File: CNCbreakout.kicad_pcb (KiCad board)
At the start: 2 copper layers, 7 parts, among them P1 X1_IN, P10 XY_STOP, P11 Z_STOP, P2 X2_IN, P5 VFD_IN, P6 X1_OUT, P7 X2_OUT

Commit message: started pcb layout
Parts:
- removed P1: X1_IN, Connect:DB25FC
- removed P10: XY_STOP, Connect:DB9FC
- removed P11: Z_STOP, Connect:DB9FC
- removed P2: X2_IN, Connect:DB25FC
- removed P5: VFD_IN, Connect:DB9FC
- removed P6: X1_OUT, Connect:DB25MC
- removed P7: X2_OUT, Connect:DB25MC
- added D201: LED, LEDs:LED_1206, F.Cu at (279.4, 102.9)
- added D202: LED, LEDs:LED_1206, F.Cu at (269.2, 102.9)
- added D203: LED, LEDs:LED_1206, F.Cu at (259.1, 102.9)
- added D204: LED, LEDs:LED_1206, F.Cu at (248.9, 102.9)
- added D205: LED, LEDs:LED_1206, F.Cu at (238.8, 102.9)
- added D206: LED, LEDs:LED_1206, F.Cu at (228.6, 102.9)
- added D301: LED, LEDs:LED_1206, F.Cu at (39.4, 66.0)
- added D302: LED, LEDs:LED_1206, F.Cu at (57.1, 66.0)
- added D303: LED, LEDs:LED_1206, F.Cu at (96.5, 64.8)
- added D304: LED, LEDs:LED_1206, F.Cu at (114.3, 64.8)
- added D305: LED, LEDs:LED_1206, F.Cu at (151.1, 64.8)
- added D306: LED, LEDs:LED_1206, F.Cu at (166.4, 64.8)
- added D307: LED, LEDs:LED_1206, F.Cu at (39.4, 58.4)
- added D308: LED, LEDs:LED_1206, F.Cu at (57.1, 58.4)
- added D309: LED, LEDs:LED_1206, F.Cu at (96.5, 58.4)
- added D310: LED, LEDs:LED_1206, F.Cu at (114.3, 58.4)
- added D311: LED, LEDs:LED_1206, F.Cu at (151.1, 58.4)
- added D312: LED, LEDs:LED_1206, F.Cu at (166.4, 58.4)
- added D313: LED, LEDs:LED_1206, F.Cu at (158.8, 62.2)
- added D314: LED, LEDs:LED_1206, F.Cu at (48.3, 62.2)
- added D315: LED, LEDs:LED_1206, F.Cu at (105.4, 62.2)
- added P101: X1, Connect:DB9FC, F.Cu at (47.0, 133.3)
- added P102: X2, Connect:DB9FC, F.Cu at (85.1, 133.3)
- added P103: Y, Connect:DB9FC, F.Cu at (123.2, 133.3)
- added P104: Z, Connect:DB9FC, F.Cu at (161.3, 133.3)
- added P105: GND, Connect:bornier2, F.Cu at (256.5, 48.3)
- added P106: +24V, Connect:bornier2, F.Cu at (268.0, 33.0)
- added P110: CONN_01X02, Connect:bornier2, F.Cu at (273.1, 77.5)
- added P111: CONN_01X02, Connect:bornier2, F.Cu at (254.0, 77.5)
- added P112: CONN_01X02, Connect:bornier2, F.Cu at (233.7, 77.5)
- added Q201: Q_NMOS_GDS, TO_SOT_Packages_SMD:TO-252-2Lead, F.Cu at (279.4, 95.2)
- added Q202: Q_NMOS_GDS, TO_SOT_Packages_SMD:TO-252-2Lead, F.Cu at (269.2, 95.2)
- added Q203: Q_NMOS_GDS, TO_SOT_Packages_SMD:TO-252-2Lead, F.Cu at (259.1, 95.2)
- added Q204: Q_NMOS_GDS, TO_SOT_Packages_SMD:TO-252-2Lead, F.Cu at (248.9, 95.2)
- added Q205: Q_NMOS_GDS, TO_SOT_Packages_SMD:TO-252-2Lead, F.Cu at (238.8, 95.2)
- added Q206: Q_NMOS_GDS, TO_SOT_Packages_SMD:TO-252-2Lead, F.Cu at (228.6, 95.2)
- added Q301: Q_NPN_CBE, TO_SOT_Packages_SMD:SOT-23, F.Cu at (41.9, 96.5)
- added Q302: Q_NPN_CBE, TO_SOT_Packages_SMD:SOT-23, F.Cu at (61.0, 96.5)
- added Q303: Q_NPN_CBE, TO_SOT_Packages_SMD:SOT-23, F.Cu at (43.2, 83.8)
- added Q304: Q_NPN_CBE, TO_SOT_Packages_SMD:SOT-23, F.Cu at (61.0, 83.8)
- added Q305: Q_NPN_CBE, TO_SOT_Packages_SMD:SOT-23, F.Cu at (95.2, 85.1)
- added Q306: Q_NPN_CBE, TO_SOT_Packages_SMD:SOT-23, F.Cu at (114.3, 85.1)
- added Q307: Q_NPN_CBE, TO_SOT_Packages_SMD:SOT-23, F.Cu at (149.9, 85.1)
- added Q308: Q_NPN_CBE, TO_SOT_Packages_SMD:SOT-23, F.Cu at (167.6, 85.1)
- added R201: 2K, Resistors_SMD:R_1206, F.Cu at (278.1, 99.1)
- added R202: 2K, Resistors_SMD:R_1206, F.Cu at (276.9, 108.0)
- added R203: 2K, Resistors_SMD:R_1206, F.Cu at (268.0, 99.1)
- added R204: 2K, Resistors_SMD:R_1206, F.Cu at (266.7, 108.0)
- added R205: 2K, Resistors_SMD:R_1206, F.Cu at (257.8, 99.1)
- added R206: 2K, Resistors_SMD:R_1206, F.Cu at (256.5, 108.0)
- added R207: 2K, Resistors_SMD:R_1206, F.Cu at (247.7, 99.1)
- added R208: 2K, Resistors_SMD:R_1206, F.Cu at (246.4, 108.0)
- added R209: 2K, Resistors_SMD:R_1206, F.Cu at (237.5, 99.1)
- added R210: 2K, Resistors_SMD:R_1206, F.Cu at (236.2, 108.0)
- added R211: 2K, Resistors_SMD:R_1206, F.Cu at (227.3, 99.1)
- added R212: 2K, Resistors_SMD:R_1206, F.Cu at (226.1, 108.0)
- added R303: 5K, Resistors_SMD:R_1206, F.Cu at (40.6, 90.2)
- added R304: 5K, Resistors_SMD:R_1206, F.Cu at (58.4, 90.2)
- added R305: 5K, Resistors_SMD:R_1206, F.Cu at (92.7, 92.7)
- added R306: 5K, Resistors_SMD:R_1206, F.Cu at (111.8, 92.7)
- added R307: 5K, Resistors_SMD:R_1206, F.Cu at (147.3, 92.7)
- added R308: 5K, Resistors_SMD:R_1206, F.Cu at (165.1, 92.7)
- added R309: 5K, Resistors_SMD:R_1206, F.Cu at (41.9, 72.4)
- added R310: 5K, Resistors_SMD:R_1206, F.Cu at (55.9, 72.4)
- added R311: 5K, Resistors_SMD:R_1206, F.Cu at (100.3, 71.1)
- added R312: 5K, Resistors_SMD:R_1206, F.Cu at (113.0, 71.1)
- added R313: 5K, Resistors_SMD:R_1206, F.Cu at (153.7, 71.1)
- added R314: 5K, Resistors_SMD:R_1206, F.Cu at (166.4, 71.1)
- added R315: 2K5, Resistors_SMD:R_1206, F.Cu at (45.7, 90.2)
- added R316: 2K5, Resistors_SMD:R_1206, F.Cu at (63.5, 90.2)
- added R317: 5K, Resistors_SMD:R_1206, F.Cu at (97.8, 92.7)
- added R318: 5K, Resistors_SMD:R_1206, F.Cu at (116.8, 92.7)
- added R319: 5K, Resistors_SMD:R_1206, F.Cu at (152.4, 92.7)
- added R320: 5K, Resistors_SMD:R_1206, F.Cu at (170.2, 92.7)
- added R321: 10K, Resistors_SMD:R_1206, F.Cu at (48.3, 83.8)
- added R322: 10K, Resistors_SMD:R_1206, F.Cu at (66.0, 83.8)
- added R323: 10K, Resistors_SMD:R_1206, F.Cu at (100.3, 85.1)
- added R324: 10K, Resistors_SMD:R_1206, F.Cu at (119.4, 85.1)
- added R325: 10K, Resistors_SMD:R_1206, F.Cu at (154.9, 85.1)
- added R326: 10K, Resistors_SMD:R_1206, F.Cu at (172.7, 85.1)
- added R327: 10K, Resistors_SMD:R_1206, F.Cu at (35.6, 72.4)
- added R328: 10K, Resistors_SMD:R_1206, F.Cu at (61.0, 72.4)
- added R329: 10K, Resistors_SMD:R_1206, F.Cu at (94.0, 71.1)
- added R330: 10K, Resistors_SMD:R_1206, F.Cu at (118.1, 71.1)
- added R331: 10K, Resistors_SMD:R_1206, F.Cu at (147.3, 71.1)
- added R332: 10K, Resistors_SMD:R_1206, F.Cu at (172.7, 71.1)
- added R333: 10K, Resistors_SMD:R_1206, F.Cu at (194.3, 26.7)
- added R334: 10K, Resistors_SMD:R_1206, F.Cu at (194.3, 33.0)
- added R335: 10K, Resistors_SMD:R_1206, F.Cu at (106.7, 71.1)
- added R336: 10K, Resistors_SMD:R_1206, F.Cu at (160.0, 71.1)
- added R337: 10K, Resistors_SMD:R_1206, F.Cu at (49.5, 72.4)
- added R338: 100K, Resistors_SMD:R_1206, F.Cu at (212.1, 33.0)
- added R339: 100K, Resistors_SMD:R_1206, F.Cu at (212.1, 26.7)
- added U301: 4N25, Opto-Devices:Optocoupler_SMD_ReflowWaveSoldering_KPC357_LTV35x_PC357_SingleChannel, F.Cu at (203.2, 27.9)
- added U302: 4N25, Opto-Devices:Optocoupler_SMD_ReflowWaveSoldering_KPC357_LTV35x_PC357_SingleChannel, F.Cu at (203.2, 34.3)

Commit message: added opto and DE footprints
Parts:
- added P107: Z_STOP, CNCbreakout:DE15HDFC, F.Cu at (22.9, 48.3)
- added P108: XY_STOP, CNCbreakout:DE15HDFC, F.Cu at (22.9, 96.5)
- added P109: VFD_IN, CNCbreakout:DE15HDFC, F.Cu at (207.0, 138.4)
- added R601: R, Resistors_SMD:R_1206, F.Cu at (35.6, 120.7)
- added R602: R, Resistors_SMD:R_1206, F.Cu at (73.7, 120.7)
- added R603: R, Resistors_SMD:R_1206, F.Cu at (111.8, 120.7)
- added R604: R, Resistors_SMD:R_1206, F.Cu at (151.1, 120.7)
- added U601: TCMT1108, CNCbreakout:TCMT1108, F.Cu at (36.8, 124.5)
- added U602: TCMT1108, CNCbreakout:TCMT1108, F.Cu at (74.9, 124.5)
- added U603: TCMT1108, CNCbreakout:TCMT1108, F.Cu at (113.0, 124.5)
- added U604: TCMT1108, CNCbreakout:TCMT1108, F.Cu at (152.4, 124.5)
- P101, P102, P103, P104: footprint Connect:DB9FC -> CNCbreakout:DE9FC
- U301, U302: value 4N25 -> TCMT1108; footprint Opto-Devices:Optocoupler_SMD_ReflowWaveSoldering_KPC357_LTV35x_PC357_SingleChannel -> CNCbreakout:TCMT1108
- moved R202 66.1 mm to (210.8, 109.2), turned to 180 degrees
- moved D201 64.1 mm to (215.9, 111.8), turned to 90 degrees
- moved R201 59.5 mm to (219.7, 110.5), turned to 90 degrees
- moved Q201 58.3 mm to (223.5, 111.8), turned to 270 degrees
- moved R204 56.6 mm to (210.8, 99.1), turned to 180 degrees
- moved D202 53.4 mm to (215.9, 101.6), turned to 90 degrees
- moved R212 51.8 mm to (210.8, 58.4), turned to 180 degrees
- moved R206 49.5 mm to (210.8, 88.9), turned to 180 degrees
- moved R203 48.3 mm to (219.7, 100.3), turned to 90 degrees
- moved R210 46.9 mm to (210.8, 68.6), turned to 180 degrees
- moved Q202 46.2 mm to (223.5, 101.6), turned to 270 degrees
- moved R208 46.0 mm to (210.8, 78.7), turned to 180 degrees
- moved D203 44.7 mm to (215.9, 91.4), turned to 90 degrees
- moved D206 43.8 mm to (215.9, 61.0), turned to 270 degrees
- moved P110 42.3 mm to (241.3, 105.4), turned to 270 degrees
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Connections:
- P101 pad 4: Net-(P101-Pad4) -> /Estop_Logic/X1EN+
- P101 pad 5: Net-(P101-Pad5) -> /Estop_Logic/X1EN-
- P102 pad 4: Net-(P102-Pad4) -> /Estop_Logic/X2EN+
- P102 pad 5: Net-(P102-Pad5) -> /Estop_Logic/X2EN-
- P103 pad 4: Net-(P103-Pad4) -> /Estop_Logic/YEN+
- P103 pad 5: Net-(P103-Pad5) -> /Estop_Logic/YEN-
- P104 pad 4: Net-(P104-Pad4) -> /Estop_Logic/ZEN+
- P104 pad 5: Net-(P104-Pad5) -> /Estop_Logic/ZEN-
- U301 pad 3: (no net) -> DGND
- U301 pad 4: DGND -> DOut_1
- U302 pad 3: (no net) -> DGND
- U302 pad 4: DGND -> DOut_2

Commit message: set limits to pull down, optional invert
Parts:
- added D316: ZENERsmall, Diodes_SMD:SOD-123, F.Cu at (123.0, 82.0)
- added D317: ZENERsmall, Diodes_SMD:SOD-123, F.Cu at (147.0, 82.0)
- added D318: ZENERsmall, Diodes_SMD:SOD-123, F.Cu at (171.0, 82.0)
- added D319: LED, LEDs:LED_1206, F.Cu at (153.0, 69.0)
- added D320: LED, LEDs:LED_1206, F.Cu at (57.0, 69.0)
- added D321: LED, LEDs:LED_1206, F.Cu at (105.0, 69.0)
- added JP301: JUMPER3, CNCbreakout:JumperDouble, F.Cu at (44.0, 89.0)
- added JP302: JUMPER3, CNCbreakout:JumperDouble, F.Cu at (68.0, 89.0)
- added JP303: JUMPER3, CNCbreakout:JumperDouble, F.Cu at (92.0, 89.0)
- added JP304: JUMPER3, CNCbreakout:JumperDouble, F.Cu at (116.0, 89.0)
- added JP305: JUMPER3, CNCbreakout:JumperDouble, F.Cu at (140.0, 89.0)
- added JP306: JUMPER3, CNCbreakout:JumperDouble, F.Cu at (164.0, 89.0)
- added Q309: Q_NPN_CBE, TO_SOT_Packages_SMD:SOT-23, F.Cu at (98.0, 94.0)
- added Q310: Q_NPN_CBE, TO_SOT_Packages_SMD:SOT-23, F.Cu at (122.0, 94.0)
- added Q311: Q_NPN_CBE, TO_SOT_Packages_SMD:SOT-23, F.Cu at (146.0, 94.0)
- added Q312: Q_NPN_CBE, TO_SOT_Packages_SMD:SOT-23, F.Cu at (170.0, 94.0)
- added Q313: Q_NPN_CBE, TO_SOT_Packages_SMD:SOT-23, F.Cu at (50.0, 86.0)
- added Q314: Q_NPN_CBE, TO_SOT_Packages_SMD:SOT-23, F.Cu at (74.0, 86.0)
- added Q315: Q_NPN_CBE, TO_SOT_Packages_SMD:SOT-23, F.Cu at (98.0, 86.0)
- added Q316: Q_NPN_CBE, TO_SOT_Packages_SMD:SOT-23, F.Cu at (122.0, 86.0)
- added Q317: Q_NPN_CBE, TO_SOT_Packages_SMD:SOT-23, F.Cu at (146.0, 86.0)
- added Q318: Q_NPN_CBE, TO_SOT_Packages_SMD:SOT-23, F.Cu at (170.0, 86.0)
- added R301: 5K, Resistors_SMD:R_1206, F.Cu at (44.0, 100.0)
- added R302: 5K, Resistors_SMD:R_1206, F.Cu at (68.0, 100.0)
- added R340: 5K, Resistors_SMD:R_1206, F.Cu at (111.0, 79.0)
- added R341: 5K, Resistors_SMD:R_1206, F.Cu at (135.0, 79.0)
- added R342: 5K, Resistors_SMD:R_1206, F.Cu at (159.0, 79.0)
- added R343: 10K, Resistors_SMD:R_1206, F.Cu at (47.0, 79.0)
- added R344: 10K, Resistors_SMD:R_1206, F.Cu at (71.0, 79.0)
- added R345: 10K, Resistors_SMD:R_1206, F.Cu at (95.0, 79.0)
- added R346: 10K, Resistors_SMD:R_1206, F.Cu at (119.0, 79.0)
- added R347: 10K, Resistors_SMD:R_1206, F.Cu at (143.0, 79.0)
- added R348: 10K, Resistors_SMD:R_1206, F.Cu at (167.0, 79.0)
- added R349: 10K, Resistors_SMD:R_1206, F.Cu at (207.5, 117.5)
- added R350: 10K, Resistors_SMD:R_1206, F.Cu at (201.5, 118.0)
- added R351: 10K, Resistors_SMD:R_1206, F.Cu at (108.0, 75.0)
- added R352: 10K, Resistors_SMD:R_1206, F.Cu at (156.0, 75.0)
- added R353: 10K, Resistors_SMD:R_1206, F.Cu at (60.0, 75.0)
- D313, D314, D315: value LED -> ZENERsmall; footprint LEDs:LED_1206 -> Diodes_SMD:SOD-123
- P107: value Z_STOP -> CONN_01X02; footprint CNCbreakout:DE15HDFC -> Connect:bornier2
- P108: value XY_STOP -> CONN_01X02; footprint CNCbreakout:DE15HDFC -> Connect:bornier2
- P109: value VFD_IN -> CONN_01X02; footprint CNCbreakout:DE15HDFC -> Connect:bornier2
- P110: value CONN_01X02 -> Z_STOP; footprint Connect:bornier2 -> CNCbreakout:DE15HDFC
- P111: value CONN_01X02 -> XY_STOP; footprint Connect:bornier2 -> CNCbreakout:DE15HDFC
- P112: value CONN_01X02 -> VFD_IN; footprint Connect:bornier2 -> CNCbreakout:DE15HDFC
- R307, R308, R309, R310, R311, R312: value 5K -> 20K
- R313, R314, R317, R318: value 5K -> 10K
- R315, R316: value 2K5 -> 10K
- R321, R322, R323, R324, R331, R332, R333, R334, R335, R336: value 10K -> 5K
- R338: value 100K -> 10K
- R339: value 100K -> 5K
- moved P107 228.8 mm to (244.0, 107.0), turned to 270 degrees
- moved P111 224.7 mm to (18.0, 111.0), turned to 90 degrees
- moved P110 224.1 mm to (19.0, 77.0), turned to 90 degrees
- moved P108 221.4 mm to (244.0, 85.5), turned to 270 degrees
- moved R338 156.0 mm to (63.0, 79.0)
- moved R339 135.6 mm to (87.0, 79.0)
- moved R333 121.2 mm to (87.0, 83.0), turned to 0 degrees
- moved R313 114.8 mm to (39.0, 89.0)
- moved R319 113.4 mm to (39.0, 95.0), turned to 180 degrees
- moved D313 109.5 mm to (51.0, 82.0), turned to 180 degrees
- moved R332 109.1 mm to (63.0, 83.0), turned to 0 degrees
- moved R307 108.5 mm to (39.0, 99.0), turned to 0 degrees
- moved R331 107.7 mm to (39.0, 83.0), turned to 180 degrees
- moved R320 107.2 mm to (63.0, 95.0), turned to 180 degrees
- moved R314 103.7 mm to (63.0, 89.0)
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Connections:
- D307 pad 1: Net-(D307-Pad1) -> GND
- D307 pad 2: LimX+ -> Net-(D307-Pad2)
- D308 pad 1: Net-(D308-Pad1) -> GND
- D308 pad 2: LimX- -> Net-(D308-Pad2)
- D309 pad 1: Net-(D309-Pad1) -> GND
- D309 pad 2: LimY+ -> Net-(D309-Pad2)
- D310 pad 1: Net-(D310-Pad1) -> GND
- D310 pad 2: LimY- -> Net-(D310-Pad2)
- D311 pad 1: Net-(D311-Pad1) -> GND
- D311 pad 2: LimZ+ -> Net-(D311-Pad2)
- D312 pad 1: Net-(D312-Pad1) -> GND
- D312 pad 2: LimZ- -> Net-(D312-Pad2)
- D313 pad 1: HomeZ -> Net-(D313-Pad1)
- D313 pad 2: Net-(D313-Pad2) -> GND
- D314 pad 1: HomeX -> Net-(D314-Pad1)
- D314 pad 2: Net-(D314-Pad2) -> GND
- D315 pad 1: HomeY -> Net-(D315-Pad1)
- D315 pad 2: Net-(D315-Pad2) -> GND
- P101 pad 6: +24V -> Net-(P101-Pad6)
- P102 pad 6: +24V -> Net-(P102-Pad6)
- P103 pad 6: +24V -> Net-(P103-Pad6)
- P104 pad 6: +24V -> Net-(P104-Pad6)
- P107 pad 1: GND -> /vfd_aux/GPO2
- P107 pad 2: SOL1 -> /vfd_aux/GPO1
- P108 pad 1: GND -> /vfd_aux/GPO4
- P108 pad 2: LimY+ -> /vfd_aux/GPO3
- P109 pad 1: +24V -> /vfd_aux/GPO6
- P109 pad 2: DIn_1 -> /vfd_aux/GPO5
- P110 pad 1: /vfd_aux/GPO2 -> GND
- P110 pad 2: /vfd_aux/GPO1 -> SOL1
- P111 pad 1: /vfd_aux/GPO4 -> GND
- P111 pad 2: /vfd_aux/GPO3 -> LimY+
- P112 pad 1: /vfd_aux/GPO6 -> +24V
- P112 pad 2: /vfd_aux/GPO5 -> DIn_1
- Q303 pad 1: Net-(Q303-Pad1) -> Y+Lim
- Q304 pad 1: Net-(Q304-Pad1) -> Y-Lim
- Q305 pad 1: Net-(Q305-Pad1) -> Z+Lim
- Q306 pad 1: Net-(Q306-Pad1) -> Z-Lim
- Q307 pad 1: Net-(Q307-Pad1) -> Net-(D301-Pad2)
- Q308 pad 1: Net-(Q308-Pad1) -> Net-(D302-Pad2)
- R303 pad 1: Net-(Q303-Pad1) -> Y+Lim
- R303 pad 2: Net-(Q301-Pad2) -> GND
- R304 pad 1: Net-(Q304-Pad1) -> Y-Lim
- R304 pad 2: Net-(Q302-Pad2) -> GND
- R305 pad 1: Net-(Q305-Pad1) -> Z+Lim
- R305 pad 2: Y+Lim -> GND
- R306 pad 1: Net-(Q306-Pad1) -> Z-Lim
- R306 pad 2: Y-Lim -> GND
- R307 pad 1: Net-(Q307-Pad1) -> +24V
- R307 pad 2: Z+Lim -> F1_LIM
- R308 pad 1: Net-(Q308-Pad1) -> +24V
- R308 pad 2: Z-Lim -> R1_LIM
- R309 pad 1: Net-(D301-Pad2) -> +24V
- R309 pad 2: Net-(Q303-Pad1) -> Y+Lim
- R310 pad 1: Net-(D302-Pad2) -> +24V
- R310 pad 2: Net-(Q304-Pad1) -> Y-Lim
- R311 pad 1: Net-(D303-Pad2) -> +24V
- R311 pad 2: Net-(Q305-Pad1) -> Z+Lim
- R312 pad 1: Net-(D304-Pad2) -> +24V
- R312 pad 2: Net-(Q306-Pad1) -> Z-Lim
- R313 pad 1: Net-(D305-Pad2) -> Net-(JP301-Pad2)
- R313 pad 2: Net-(Q307-Pad1) -> Net-(Q301-Pad2)
- R314 pad 1: Net-(D306-Pad2) -> Net-(JP302-Pad2)
- R314 pad 2: Net-(Q308-Pad1) -> Net-(Q302-Pad2)
- R315 pad 1: +24V -> Net-(JP303-Pad2)
- R315 pad 2: Net-(Q303-Pad1) -> Net-(Q303-Pad2)
- R316 pad 1: +24V -> Net-(JP304-Pad2)
- R316 pad 2: Net-(Q304-Pad1) -> Net-(Q304-Pad2)
- R317 pad 1: +24V -> Net-(JP305-Pad2)
- R317 pad 2: Net-(Q305-Pad1) -> Net-(Q305-Pad2)
- R318 pad 1: +24V -> Net-(JP306-Pad2)
- R318 pad 2: Net-(Q306-Pad1) -> Net-(Q306-Pad2)
- R319 pad 1: +24V -> Net-(D301-Pad2)
- R319 pad 2: Net-(Q307-Pad1) -> +24V
- R320 pad 1: +24V -> Net-(D302-Pad2)
- R320 pad 2: Net-(Q308-Pad1) -> +24V
- R321 pad 1: Net-(Q303-Pad2) -> +24V
- R321 pad 2: GND -> Net-(D303-Pad2)
- R322 pad 1: Net-(Q304-Pad2) -> +24V
- R322 pad 2: GND -> Net-(D304-Pad2)
- R323 pad 1: Net-(Q305-Pad2) -> +24V
- R323 pad 2: GND -> Net-(D305-Pad2)
- R324 pad 1: Net-(Q306-Pad2) -> +24V
- R324 pad 2: GND -> Net-(D306-Pad2)
- R325 pad 1: Net-(Q307-Pad2) -> Net-(D307-Pad2)
- R325 pad 2: GND -> Net-(Q307-Pad2)
- R326 pad 1: Net-(Q308-Pad2) -> Net-(D308-Pad2)
- R326 pad 2: GND -> Net-(Q308-Pad2)
- R327 pad 1: Net-(D307-Pad1) -> Net-(D309-Pad2)
- R327 pad 2: Net-(Q303-Pad2) -> Net-(Q309-Pad2)
- R328 pad 1: Net-(D308-Pad1) -> Net-(D310-Pad2)
- R328 pad 2: Net-(Q304-Pad2) -> Net-(Q310-Pad2)
- R329 pad 1: Net-(D309-Pad1) -> Net-(D311-Pad2)
- R329 pad 2: Net-(Q305-Pad2) -> Net-(Q311-Pad2)
- R330 pad 1: Net-(D310-Pad1) -> Net-(D312-Pad2)
- R330 pad 2: Net-(Q306-Pad2) -> Net-(Q312-Pad2)
- R331 pad 1: Net-(D311-Pad1) -> Net-(D307-Pad2)
- R331 pad 2: Net-(Q307-Pad2) -> +24V
- R332 pad 1: Net-(D312-Pad1) -> +24V
- R332 pad 2: Net-(Q308-Pad2) -> Net-(D308-Pad2)
- R333 pad 1: Net-(R333-Pad1) -> +24V
- R333 pad 2: +24V -> Net-(D309-Pad2)
- R334 pad 1: Net-(R334-Pad1) -> +24V
- R334 pad 2: +24V -> Net-(D310-Pad2)
- R335 pad 2: Net-(D315-Pad2) -> Net-(D311-Pad2)
- R336 pad 2: Net-(D313-Pad2) -> Net-(D312-Pad2)
- R337 pad 1: +24V -> LimX+
- R337 pad 2: Net-(D314-Pad2) -> +24V
- R338 pad 1: Net-(R338-Pad1) -> LimX-
- R338 pad 2: DGND -> +24V
- R339 pad 1: Net-(R339-Pad1) -> LimY+
- R339 pad 2: DGND -> +24V
- U301 pad 1: Net-(R333-Pad1) -> Net-(R349-Pad1)
- U302 pad 1: Net-(R334-Pad1) -> Net-(R350-Pad1)
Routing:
- net GND: track 0.00 -> 370.9 mm
- net +24V: track 0.00 -> 136.1 mm
- net Net-(Q301-Pad2): track 0.00 -> 23.8 mm
- net Net-(Q304-Pad2): track 0.00 -> 23.8 mm
- net Net-(Q303-Pad2): track 0.00 -> 23.8 mm
- net Net-(Q302-Pad2): track 0.00 -> 23.8 mm
- net Net-(Q306-Pad2): track 0.00 -> 23.8 mm
- net Net-(Q305-Pad2): track 0.00 -> 23.8 mm
- net Net-(D308-Pad2): track 0.00 -> 19.0 mm
- net Net-(D312-Pad2): track 0.00 -> 19.0 mm
- net Net-(D311-Pad2): track 0.00 -> 19.0 mm
- net Net-(D307-Pad2): track 0.00 -> 19.0 mm
- net Net-(D310-Pad2): track 0.00 -> 19.0 mm
- net Net-(D309-Pad2): track 0.00 -> 19.0 mm
- net Net-(D306-Pad2): track 0.00 -> 16.2 mm
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
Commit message: closer to full routing
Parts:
- P101, P102, P103, P104, P105, P106, P107, P108, P109, P110, P111, P112: moved to B.Cu
- moved P106 90.3 mm to (202.0, 113.0)
- moved P105 70.5 mm to (202.0, 103.0)
- moved R349 45.3 mm to (164.0, 130.0)
- moved D206 45.0 mm to (172.0, 71.0), turned to 90 degrees
- moved R211 44.9 mm to (176.0, 70.0)
- moved Q206 44.7 mm to (180.0, 71.0)
- moved D205 44.6 mm to (172.0, 79.0)
- moved R209 44.5 mm to (176.0, 78.0)
- moved P107 44.3 mm to (202.0, 93.0)
- moved D204 44.3 mm to (172.0, 87.0)
- moved Q205 44.2 mm to (180.0, 79.0)
- moved R207 44.1 mm to (176.0, 86.0)
- moved D203 44.0 mm to (172.0, 95.0)
- moved D202 43.9 mm to (172.0, 103.0)
- moved D201 43.9 mm to (172.0, 111.0)
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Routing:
- net LimZ-: track 5.10 -> 138.7 mm, vias 0 -> 2
- net LimY-: track 5.10 -> 121.2 mm, vias 0 -> 2
- net GND: track 370.9 -> 481.6 mm, vias 0 -> 6
- net LimZ+: track 5.10 -> 113.7 mm
- net LimY+: track 5.10 -> 95.7 mm
- net HomeX: track 0.00 -> 86.3 mm, vias 0 -> 2
- net LimX-: track 5.10 -> 79.2 mm, vias 0 -> 2
- net F1_LIM: track 8.80 -> 75.4 mm, vias 0 -> 2
- net R1_LIM: track 8.80 -> 73.9 mm
- net DIn_6: track 0.00 -> 62.3 mm
- net HomeY: track 0.00 -> 59.2 mm
- net HomeZ: track 0.00 -> 52.2 mm
- net DIn_5: track 0.00 -> 51.9 mm
- net LimX+: track 5.10 -> 54.2 mm
- net Y+Lim: track 8.80 -> 53.3 mm
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
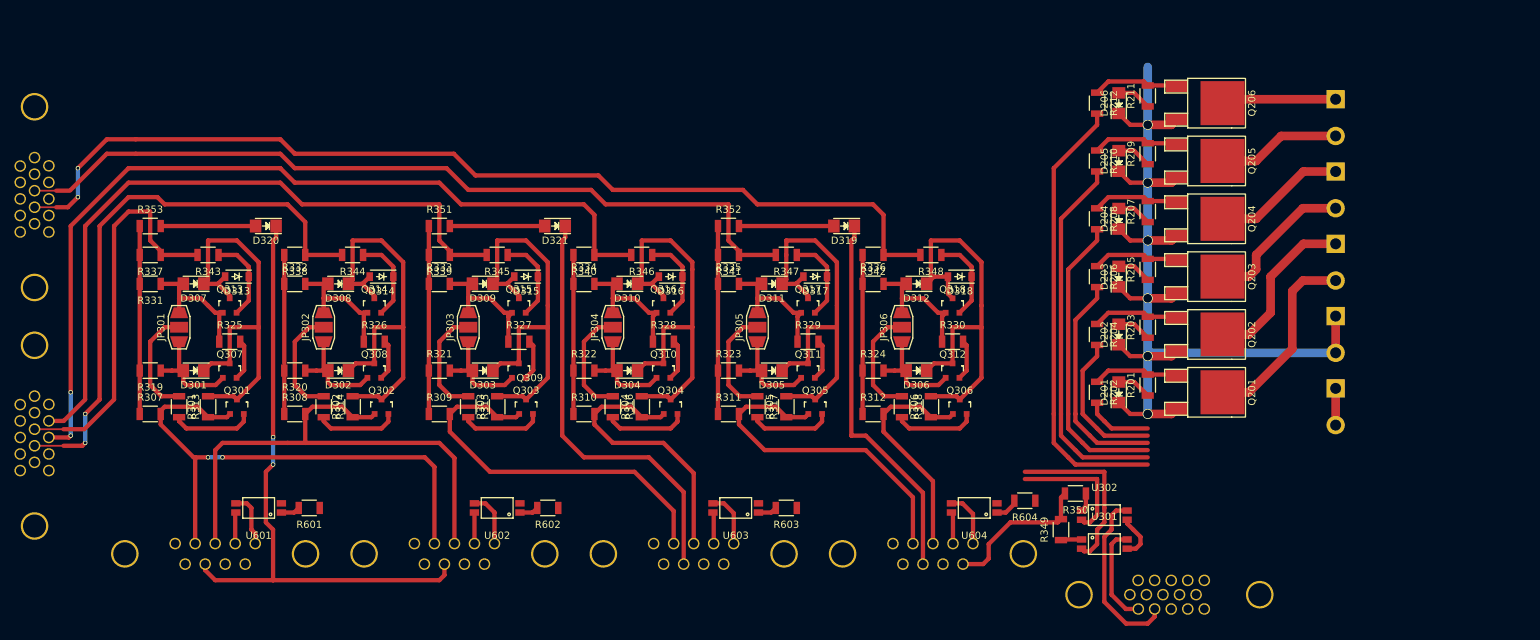
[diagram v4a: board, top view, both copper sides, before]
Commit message: adjusted DE15 footprint, added aux Z-stage lines
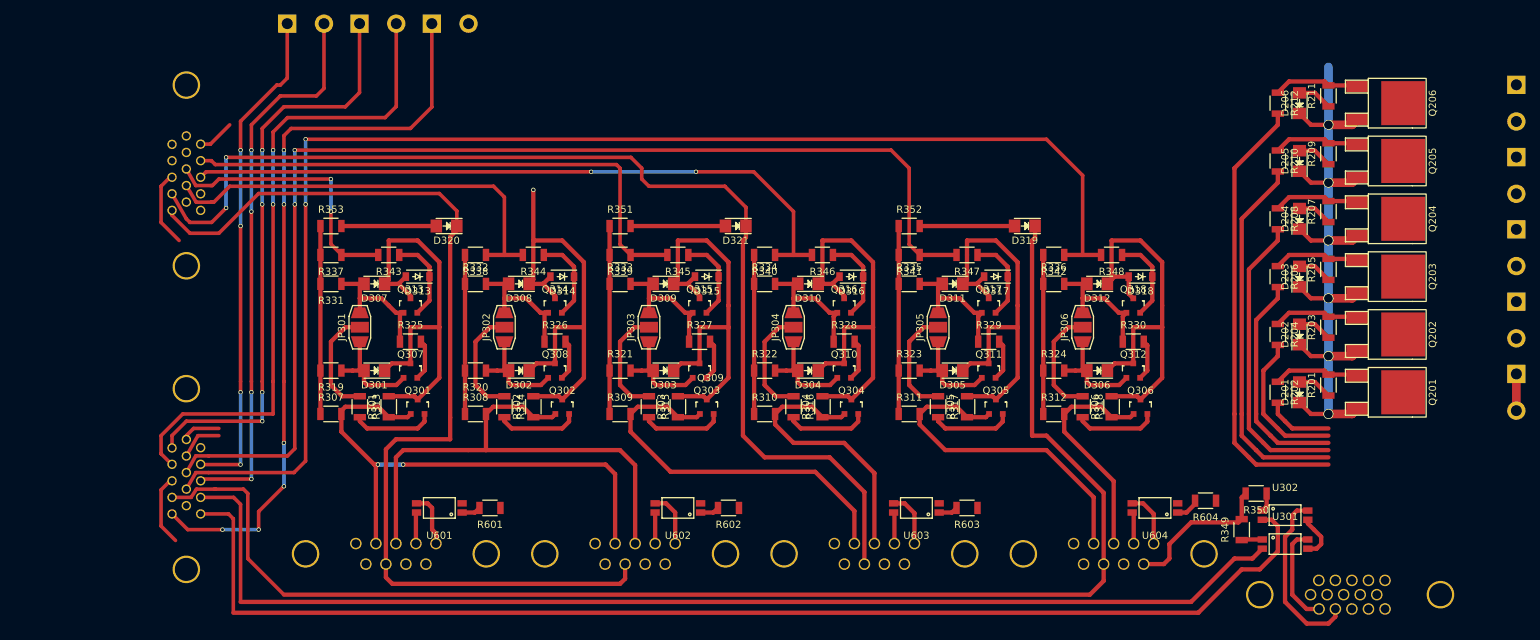
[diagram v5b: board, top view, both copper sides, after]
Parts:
- added P113: Zaux1, Connect:bornier2, B.Cu at (59.5, 60.0)
- added P114: Zaux2, Connect:bornier2, B.Cu at (69.5, 60.0)
- added P115: Zaux3, Connect:bornier2, B.Cu at (79.5, 60.0)
- moved P106 48.9 mm to (227.0, 71.0)
- moved P110 44.3 mm to (43.0, 123.0)
- moved P111 41.7 mm to (43.0, 81.0)
- moved P105 26.2 mm to (227.0, 111.0)
- moved P107 26.2 mm to (227.0, 101.0)
- moved P108 26.2 mm to (227.0, 91.0)
- moved P109 26.2 mm to (227.0, 81.0)
- moved D201 25.0 mm to (197.0, 111.0)
- moved D202 25.0 mm to (197.0, 103.0)
- moved D203 25.0 mm to (197.0, 95.0)
- moved D204 25.0 mm to (197.0, 87.0)
- moved D205 25.0 mm to (197.0, 79.0)
- moved D206 25.0 mm to (197.0, 71.0)
- moved D301 25.0 mm to (69.0, 108.0)
- moved D302 25.0 mm to (89.0, 108.0)
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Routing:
- net SpindleHallB: track 17.7 -> 171.8 mm
- net HomeZ: track 52.2 -> 196.1 mm
- net SpindleHallA: track 24.1 -> 163.8 mm
- net Net-(P110-Pad15): track 0.00 -> 102.5 mm, vias 0 -> 6
- net HomeY: track 59.2 -> 154.9 mm, vias 0 -> 2
- net Net-(P110-Pad12): track 0.00 -> 90.3 mm, vias 0 -> 2
- net Net-(P110-Pad11): track 0.00 -> 80.6 mm, vias 0 -> 4
- net SOL2: track 0.00 -> 77.2 mm, vias 0 -> 4
- net SOL1: track 0.00 -> 69.5 mm, vias 0 -> 4
- net HomeX: track 86.3 -> 139.3 mm, vias 2 -> 0
- net LimZ-: track 138.7 -> 188.7 mm
- net LimZ+: track 113.7 -> 162.4 mm, vias 0 -> 2
- net /vfd_aux/GPO1: track 26.7 -> 0.00 mm
- net LimY-: track 121.2 -> 95.7 mm
- net /vfd_aux/GPO2: track 23.8 -> 0.00 mm
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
